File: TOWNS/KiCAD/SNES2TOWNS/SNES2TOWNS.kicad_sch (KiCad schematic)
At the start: 18 parts, among them J1 DE9_Receptacle, J6 SNES_CONTROLLER, J8 ArduinoNANOP1_P15, J9 ArduinoNANOP16_P30, SW1 PCM13SMTR, U1 74LS157, U2 74LS157

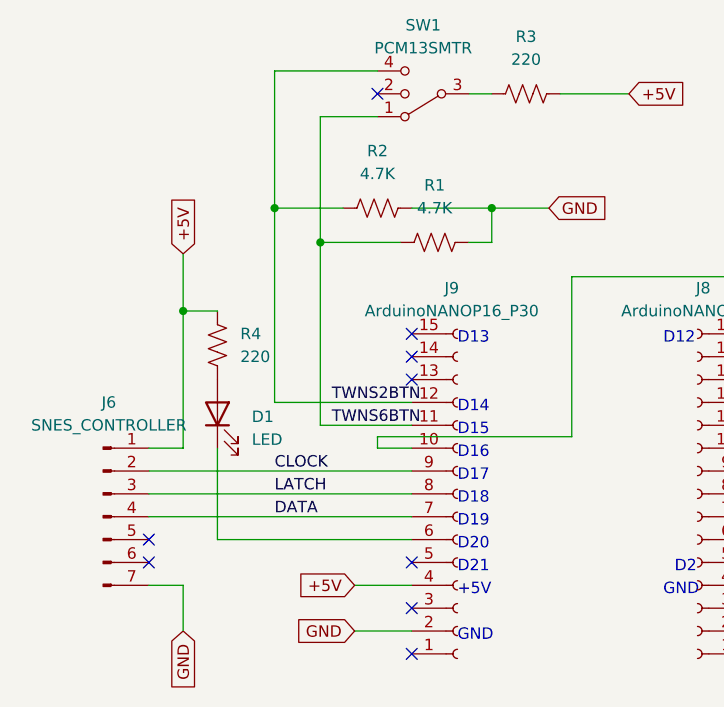
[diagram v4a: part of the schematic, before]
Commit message: Gave up status LED.
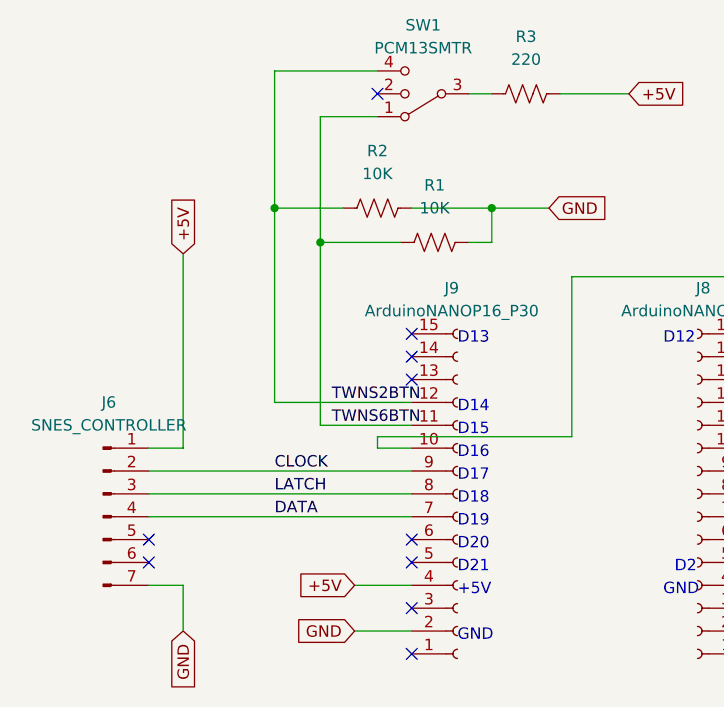
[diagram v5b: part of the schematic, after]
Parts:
- removed D1: LED, LED_SMD:LED_0805_2012Metric_Pad1.15x1.40mm_HandSolder, symbol Device:LED
- removed R4: 220, Resistor_SMD:R_0805_2012Metric_Pad1.20x1.40mm_HandSolder, symbol Device:R_US
- R1, R2: value 4.7K -> 10K
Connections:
- no-connect marks 15 -> 16
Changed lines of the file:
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@@
   (junction (at 128.27 129.54) (diameter 0) (color 0 0 0 0)
   )
-  (junction (at 53.34 73.66) (diameter 0) (color 0 0 0 0)
-  )
   (junction (at 128.27 127) (diameter 0) (color 0 0 0 0)
   )
@@
   (junction (at 162.56 139.7) (diameter 0) (color 0 0 0 0)
   )
+  (no_connect (at 78.74 99.06))
   (no_connect (at 201.93 121.92))
   (no_connect (at 115.57 111.76))
@@
     (stroke (width 0) (type default))
   )
-  (wire (pts (xy 53.34 73.66) (xy 53.34 88.9))
+  (wire (pts (xy 53.34 67.31) (xy 53.34 88.9))
     (stroke (width 0) (type default))
   )
@@
     (stroke (width 0) (type default))
   )
-  (wire (pts (xy 57.15 99.06) (xy 78.74 99.06))
-    (stroke (width 0) (type default))
-  )
   (wire (pts (xy 96.52 69.85) (xy 96.52 87.63))
     (stroke (width 0) (type default))
@@
     (stroke (width 0) (type default))
   )
-  (wire (pts (xy 53.34 67.31) (xy 53.34 73.66))
-    (stroke (width 0) (type default))
-  )
   (wire (pts (xy 49.53 93.98) (xy 78.74 93.98))
     (stroke (width 0) (type default))
@@
     (stroke (width 0) (type default))
   )
-  (wire (pts (xy 53.34 73.66) (xy 57.15 73.66))
-    (stroke (width 0) (type default))
-  )
   (wire (pts (xy 245.11 134.62) (xy 245.11 138.43))
     (stroke (width 0) (type default))
@@
   )
   (wire (pts (xy 210.82 69.85) (xy 210.82 78.74))
-    (stroke (width 0) (type default))
-  )
-  (wire (pts (xy 57.15 88.9) (xy 57.15 99.06))
     (stroke (width 0) (type default))
   )
@@
     )
   )
-  (symbol (lib_id "Device:LED") (at 57.15 85.09 90) (unit 1)
-    (in_bom yes) (on_board yes) (dnp no) (fields_autoplaced)
-    (property "Reference" "D1" (at 60.96 85.4075 90)
-      (effects (font (size 1.27 1.27)) (justify right))
-    )
-    (property "Value" "LED" (at 60.96 87.9475 90)
-      (effects (font (size 1.27 1.27)) (justify right))
-    )
-    (property "Footprint" "LED_SMD:LED_0805_2012Metric_Pad1.15x1.40mm_HandSolder" (at 57.15 85.09 0)
-      (effects (font (size 1.27 1.27)) hide)
-    )
-    (property "Datasheet" "~" (at 57.15 85.09 0)
-      (effects (font (size 1.27 1.27)) hide)
-    )
-    (pin "1")
-    (pin "2")
-    (instances
-      (project "SNES2TOWNS"
-        (path "/d12ccb08-8752-4d3d-ad3b-4f570691df19"
-          (reference "D1") (unit 1)
-        )
-      )
-    )
-  )
   (symbol (lib_id "Device:R_US") (at 147.32 121.92 90) (unit 1)
     (in_bom yes) (on_board yes) (dnp no) (fields_autoplaced)
@@
       (effects (font (size 1.27 1.27)))
     )
-    (property "Value" "4.7K" (at 74.93 58.42 90)
+    (property "Value" "10K" (at 74.93 58.42 90)
       (effects (font (size 1.27 1.27)))
     )
@@
       (effects (font (size 1.27 1.27)))
     )
-    (property "Value" "4.7K" (at 81.28 62.23 90)
+    (property "Value" "10K" (at 81.28 62.23 90)
       (effects (font (size 1.27 1.27)))
     )
@@
         )
       )
-    )
-  )
-  (symbol (lib_id "Device:R_US") (at 57.15 77.47 0) (unit 1)
-    (in_bom yes) (on_board yes) (dnp no) (fields_autoplaced)
-    (property "Reference" "R4" (at 59.69 76.2 0)
-      (effects (font (size 1.27 1.27)) (justify left))
-    )
-    (property "Value" "220" (at 59.69 78.74 0)
-      (effects (font (size 1.27 1.27)) (justify left))
-    )
-    (property "Footprint" "Resistor_SMD:R_0805_2012Metric_Pad1.20x1.40mm_HandSolder" (at 58.166 77.724 90)
-      (effects (font (size 1.27 1.27)) hide)
-    )
-    (property "Datasheet" "~" (at 57.15 77.47 0)
-      (effects (font (size 1.27 1.27)) hide)
-    )
-    (pin "1")
-    (pin "2")
-    (instances
-      (project "SNES2TOWNS"
-        (path "/d12ccb08-8752-4d3d-ad3b-4f570691df19"
-          (reference "R4") (unit 1)
-        )
-      )

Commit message: 74LS157 -> 74HC157
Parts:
- U1, U2: value 74LS157 -> 74HC157
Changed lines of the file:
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@@
       (effects (font (size 1.27 1.27)) (justify left))
     )
-    (property "Value" "74LS157" (at 191.4241 101.6 0)
+    (property "Value" "74HC157" (at 191.4241 101.6 0)
       (effects (font (size 1.27 1.27)) (justify left))
     )
@@
       (effects (font (size 1.27 1.27)) (justify left))
     )
-    (property "Value" "74LS157" (at 191.4241 41.91 0)
-      (effects (font (size 1.27 1.27)) (justify left))
-    )
+    (property "Value" "74HC157" (at 191.4241 41.91 0)
+      (effects (font (size 1.27 1.27)) (justify left))
+    )
